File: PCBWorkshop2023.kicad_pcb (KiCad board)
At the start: 2 copper layers, 70 x 38 mm, 10 parts, among them J1 Neopixel, J2 I2C, SW1 POWER SELECT, U1 TP4056, U2 WeMos_D1_mini

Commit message: Initial Routing
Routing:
- net +3V3: track 0.00 -> 59.1 mm, vias 0 -> 2
- net +4V: track 0.00 -> 47.6 mm
- net Neopixel: track 0.00 -> 34.6 mm
- net Net-(SW1-Pad1): track 0.00 -> 26.3 mm
- net Net-(BT1-Pad2): track 0.00 -> 22.8 mm
- net Net-(BT1-Pad1): track 0.00 -> 20.0 mm
- net I2C_SDA: track 0.00 -> 17.4 mm
- net I2C_CLK: track 0.00 -> 13.9 mm
- net +5V: track 0.00 -> 7.76 mm
- net (no net): track 0.00 -> 0.64 mm
- added copper zone on B.Cu, net GND
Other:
- board text added: "TODO: - Rounded corners - 90° angled switch footprint (Pusterla) - Cutout for Antenna area"
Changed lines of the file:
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@@
   )
   (gr_rect (start 111 99) (end 181 61) (layer "Edge.Cuts") (width 0.1) (fill none))
+  (gr_text "TODO:\n\n- Rounded corners\n- 90° angled switch footprint (Pusterla)\n- Cutout for Antenna area" (at 69 63) (layer "F.SilkS")
+    (effects (font (size 1 1) (thickness 0.15)) (justify left))
+  )
+  (segment (start 176.75 75.1075) (end 176.1075 75.1075) (width 0.6) (layer "B.Cu") (net 0))
+  (segment (start 165.54 62) (end 164 62) (width 1) (layer "B.Cu") (net 2))
+  (segment (start 164 62) (end 162 64) (width 1) (layer "B.Cu") (net 2))
+  (segment (start 162 64) (end 162 68) (width 1) (layer "B.Cu") (net 2))
+  (segment (start 147.3 82.7) (end 144.68 82.7) (width 1) (layer "B.Cu") (net 2))
+  (segment (start 167.54 64) (end 165.54 62) (width 1) (layer "B.Cu") (net 2))
+  (segment (start 162 68) (end 147.3 82.7) (width 1) (layer "B.Cu") (net 2))
+  (segment (start 165 66.6575) (end 165 64) (width 1) (layer "B.Cu") (net 3))
+  (segment (start 165 67.46) (end 144.68 87.78) (width 1) (layer "B.Cu") (net 3))
+  (segment (start 165 66.6575) (end 165 67.46) (width 1) (layer "B.Cu") (net 3))
+  (segment (start 174.85 73.7075) (end 174.85 72.027601) (width 1) (layer "B.Cu") (net 3))
+  (segment (start 174.85 72.027601) (end 170.282399 67.46) (width 1) (layer "B.Cu") (net 3))
+  (segment (start 173.45 75.1075) (end 174.85 73.7075) (width 1) (layer "B.Cu") (net 3))
+  (segment (start 170.282399 67.46) (end 165 67.46) (width 1) (layer "B.Cu") (net 3))
+  (segment (start 157 69) (end 157 68) (width 1) (layer "F.Cu") (net 4))
+  (segment (start 157 79) (end 157 69) (width 1) (layer "F.Cu") (net 4))
+  (via (at 157 79) (size 3) (drill 1.1) (layers "F.Cu" "B.Cu") (net 4))
+  (via (at 157 68) (size 3) (drill 1.1) (layers "F.Cu" "B.Cu") (net 4))
+  (segment (start 157 68) (end 157 64.54) (width 1) (layer "B.Cu") (net 4))
+  (segment (start 149 91) (end 156.46 83.54) (width 1) (layer "B.Cu") (net 4))
+  (segment (start 125.04 91) (end 149 91) (width 1) (layer "B.Cu") (net 4))
+  (segment (start 156.46 83.54) (end 157 83) (width 1) (layer "B.Cu") (net 4))
+  (segment (start 157 83) (end 157 79) (width 1) (layer "B.Cu") (net 4))
+  (segment (start 157 64.54) (end 156.46 64) (width 1) (layer "B.Cu") (net 4))
+  (segment (start 121.82 87.78) (end 125.04 91) (width 1) (layer "B.Cu") (net 4))
+  (segment (start 149 73.3) (end 149 68.92) (width 0.6) (layer "B.Cu") (net 5))
+  (segment (start 149 68.92) (end 153.92 64) (width 0.6) (layer "B.Cu") (net 5))
+  (segment (start 144.68 77.62) (end 149 73.3) (width 0.6) (layer "B.Cu") (net 5))
+  (segment (start 144.68 75.08) (end 148.200499 71.559501) (width 0.6) (layer "B.Cu") (net 6))
+  (segment (start 148.200499 71.559501) (end 148.200499 67.179501) (width 0.6) (layer "B.Cu") (net 6))
+  (segment (start 148.200499 67.179501) (end 151.38 64) (width 0.6) (layer "B.Cu") (net 6))
+  (segment (start 170.6075 72.6075) (end 169.5875 71.5875) (width 1) (layer "B.Cu") (net 7))
+  (segment (start 169.5875 71.5875) (end 166.1125 71.5875) (width 1) (layer "B.Cu") (net 7))
+  (segment (start 173.45 72.6075) (end 170.6075 72.6075) (width 1) (layer "B.Cu") (net 7))
+  (segment (start 170.5125 94.4875) (end 178 87) (width 1) (layer "B.Cu") (net 8))
+  (segment (start 178 82.1575) (end 173.45 77.6075) (width 1) (layer "B.Cu") (net 8))
+  (segment (start 166.1125 94.4875) (end 170.5125 94.4875) (width 1) (layer "B.Cu") (net 8))
+  (segment (start 178 87) (end 178 82.1575) (width 1) (layer "B.Cu") (net 8))
+  (segment (start 176.1 84.3) (end 172.4 88) (width 1) (layer "B.Cu") (net 9))
+  (segment (start 172.4 88) (end 165.130666 88) (width 1) (layer "B.Cu") (net 9))
+  (segment (start 165.130666 88) (end 162.6125 90.518166) (width 1) (layer "B.Cu") (net 9))
+  (segment (start 162.6125 90.518166) (end 162.6125 94.4875) (width 1) (layer "B.Cu") (net 9))
+  (segment (start 155.0125 94.4875) (end 156.5125 94.4875) (width 1) (layer "B.Cu") (net 10))
+  (segment (start 166.7 84.3) (end 173.6 84.3) (width 1) (layer "B.Cu") (net 10))
+  (segment (start 156.5125 94.4875) (end 166.7 84.3) (width 1) (layer "B.Cu") (net 10))
+  (zone (net 1) (net_name "GND") (layer "B.Cu") (hatch edge 0.508)
+    (connect_pads (clearance 0.508))
+    (min_thickness 0.254) (filled_areas_thickness no)
+    (fill yes (thermal_gap 0.508) (thermal_bridge_width 0.508))
+    (polygon
+      (pts
+        (xy 184 104)
+        (xy 105 104)
+        (xy 105 57)
+        (xy 184 57)
+      )
+    )
+  )
 )

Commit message: Changes with Bernd
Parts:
- added J3: Conn_01x02, Connector_PinHeader_2.54mm:PinHeader_1x02_P2.54mm_Vertical, F.Cu at (172.0, 63.0)
- added J4: Conn_01x07, Connector_PinHeader_2.54mm:PinHeader_1x07_P2.54mm_Vertical, F.Cu at (120.2, 89.3)
- J2: footprint Connector_PinHeader_2.54mm:PinHeader_1x04_P2.54mm_Vertical -> Connector_PinHeader_2.00mm:PinHeader_1x04_P2.00mm_Vertical
- moved SW1 16.5 mm to (189.7, 74.5)
- moved J1 5.18 mm to (165.0, 63.0)
- moved J2 3.16 mm to (156.0, 63.0)
- moved U2 1.55 mm to (123.0, 69.0)
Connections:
- U2 pad 1: unconnected-(U2-Pad1) -> DEEPSLEEP
- U2 pad 2: unconnected-(U2-Pad2) -> Net-(U2-Pad2)
- U2 pad 3: unconnected-(U2-Pad3) -> DEEPSLEEP
- U2 pad 4: unconnected-(U2-Pad4) -> Net-(U2-Pad4)
- U2 pad 5: unconnected-(U2-Pad5) -> Net-(U2-Pad5)
- U2 pad 6: unconnected-(U2-Pad6) -> Net-(U2-Pad6)
- U2 pad 7: unconnected-(U2-Pad7) -> Net-(U2-Pad7)
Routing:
- net DEEPSLEEP: track 0.00 -> 10.2 mm
- net +5V: track 7.76 -> 16.4 mm
- net +3V3: track 59.1 -> 64.4 mm
- net Net-(U2-Pad2): track 0.00 -> 4.64 mm
- net Net-(U2-Pad7): track 0.00 -> 2.86 mm
- net Net-(U2-Pad5): track 0.00 -> 2.86 mm
- net Net-(U2-Pad6): track 0.00 -> 2.86 mm
- net Net-(U2-Pad4): track 0.00 -> 2.86 mm
- net +4V: track 47.6 -> 49.1 mm
- net I2C_SDA: track 17.4 -> 16.2 mm
- net I2C_CLK: track 13.9 -> 12.8 mm
- net (no net): track 0.64 -> 0.00 mm
- net Neopixel: track 34.6 -> 34.1 mm
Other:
- board size 70 x 38 mm -> 70 x 39 mm
- board text added: "TODO: - Rounded corners - 90° angled switch footprint (Pusterla) - Double check Groove I2C adapter"
- board text removed: "TODO: - Rounded corners - 90° angled switch footprint (Pusterla) - Cutout for Antenna area"

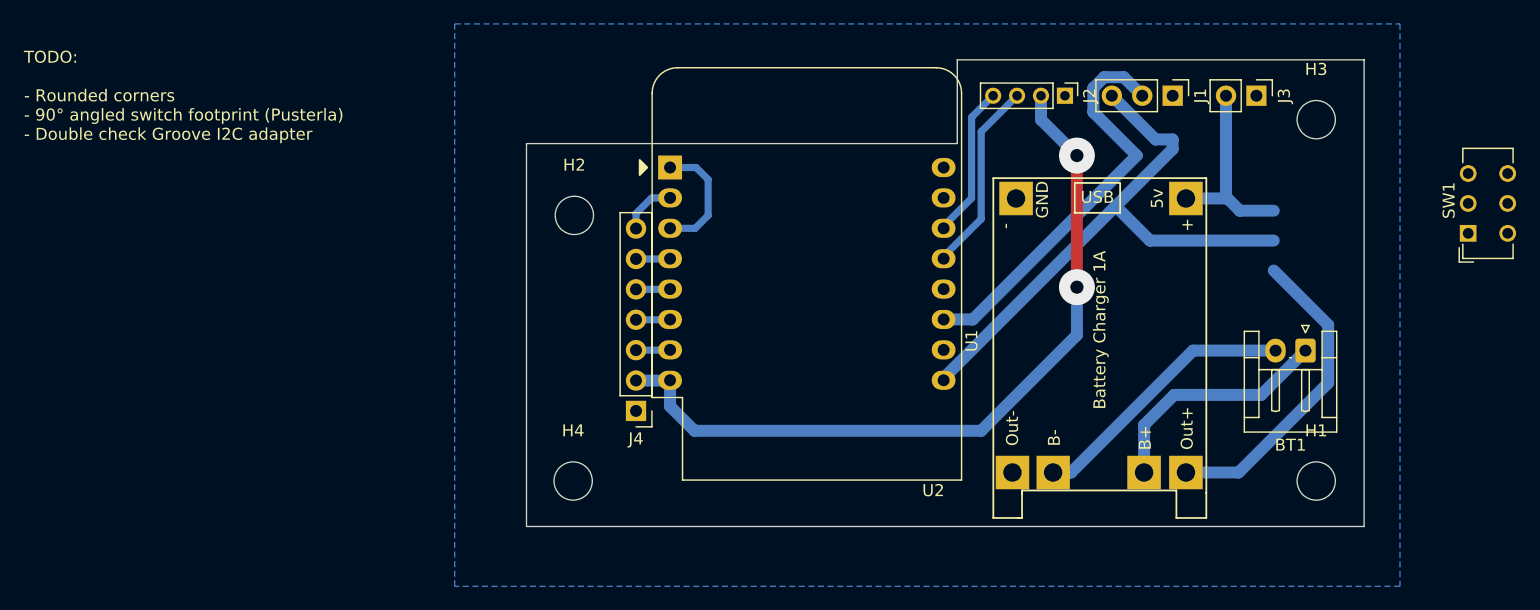
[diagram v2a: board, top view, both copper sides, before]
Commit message: Rounded corners and switch
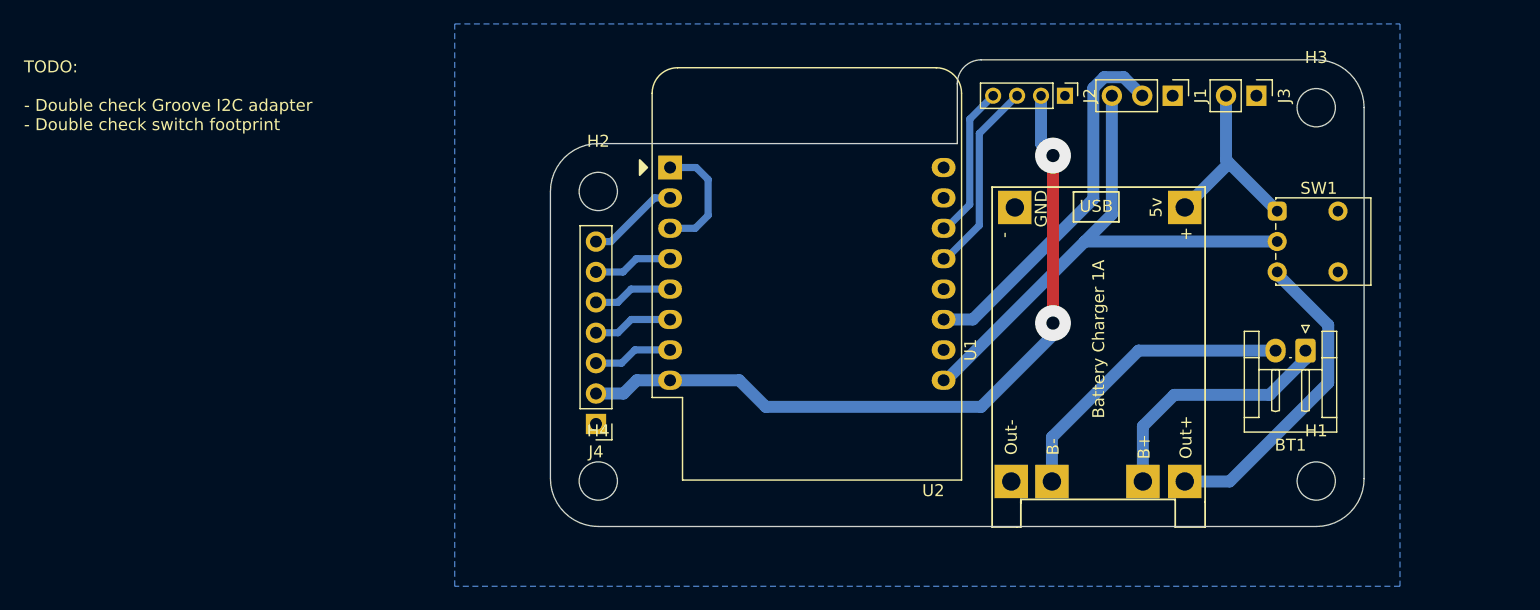
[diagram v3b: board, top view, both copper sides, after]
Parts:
- J4: value Conn_01x07 -> Connections
- SW1: footprint Button_Switch_THT:SW_CuK_JS202011CQN_DPDT_Straight -> Button_Switch_THT:SW_Push_1P2T_Vertical_E-Switch_800UDP8P1A1M6
- moved SW1 16.1 mm to (173.7, 72.6), turned to 0 degrees
- moved J4 3.52 mm to (116.8, 90.4)
- moved H2 2.83 mm to (117.0, 71.0)
- moved H4 2.10 mm to (117.0, 95.2)
- moved H3 1.00 mm to (177.0, 64.0)
- moved U1 0.76 mm to (167.7, 70.6)
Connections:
- SW1 pad 1: Net-(SW1-Pad1) -> +5V
- SW1 pad 3: +5V -> Net-(U1-Pad3)
- U1 pad 3: Net-(SW1-Pad1) -> Net-(U1-Pad3)
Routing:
- net Net-(U1-Pad3): track 0.00 -> 26.7 mm
- net Net-(SW1-Pad1): track 26.3 -> 0.00 mm
- net Net-(J4-Pad4): track 2.86 -> 6.65 mm
- net Net-(J4-Pad5): track 2.86 -> 6.65 mm
- net Net-(J4-Pad3): track 2.86 -> 6.65 mm
- net Net-(J4-Pad6): track 2.86 -> 6.65 mm
- net +4V: track 49.1 -> 46.0 mm
- net Net-(J4-Pad7): track 4.64 -> 7.70 mm
- net Neopixel: track 34.1 -> 31.1 mm
- net Net-(BT1-Pad2): track 22.8 -> 25.4 mm
- net +3V3: track 64.4 -> 62.5 mm
- net Net-(BT1-Pad1): track 20.0 -> 21.2 mm
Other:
- board size 70 x 39 mm -> 68 x 39 mm
- board text added: "TODO: - Double check Groove I2C adapter - Double check switch footprint"
- board text removed: "TODO: - Rounded corners - 90° angled switch footprint (Pusterla) - Double check Groove I2C adapter"

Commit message: Prepare for milling
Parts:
- added D1: 1N4001, Diode_THT:D_A-405_P7.62mm_Horizontal, F.Cu at (169.8, 68.7)
- SW1: value POWER SELECT -> POWER
- moved BT1 3.30 mm to (176.1, 81.0)
- moved U1 2.64 mm to (167.7, 68.0)
- moved J2 1.14 mm to (155.0, 63.5)
- moved U2 1.05 mm to (122.0, 68.9)
- moved SW1 0.98 mm to (173.0, 72.0)
- moved J1 0.80 mm to (165.1, 63.8)
- moved J3 0.75 mm to (172.0, 63.8)
- moved J4 0.37 mm to (117.0, 90.8)
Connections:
- J1 pad 3: +4V -> +5V
- J3 pad 2: +5V -> Net-(J3-Pad2)
- SW1 pad 3: Net-(U1-Pad3) -> (no net)
- U1 pad 1: +5V -> Net-(J3-Pad2)
- U1 pad 3: Net-(U1-Pad3) -> +4V
- U2 pad 9: +4V -> +5V
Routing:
- net +5V: track 16.7 -> 52.7 mm
- net Net-(U1-Pad3): track 26.7 -> 0.00 mm
- net +4V: track 46.0 -> 30.6 mm
- net Net-(J3-Pad2): track 0.00 -> 9.19 mm
- net Neopixel: track 31.1 -> 34.0 mm
- net Net-(BT1-Pad2): track 25.4 -> 23.5 mm
- net Net-(J4-Pad5): track 6.65 -> 5.58 mm
- net Net-(J4-Pad3): track 6.65 -> 5.58 mm
- net Net-(J4-Pad4): track 6.65 -> 5.58 mm
- net Net-(J4-Pad6): track 6.65 -> 5.58 mm
- net Net-(J4-Pad7): track 7.70 -> 6.64 mm

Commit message: Improvements
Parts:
- added C1: C_Polarized, Capacitor_THT:C_Radial_D6.3mm_H11.0mm_P2.50mm, F.Cu at (162.8, 68.3)
- moved U1 3.75 mm to (167.7, 71.8)
- moved J3 1.12 mm to (172.0, 62.6)
- moved J2 1.09 mm to (155.0, 62.5)
- moved J1 0.80 mm to (165.0, 63.0)
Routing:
- net +5V: track 52.7 -> 60.4 mm
- net Net-(BT1-Pad1): track 21.3 -> 25.1 mm
- net Net-(BT1-Pad2): track 23.5 -> 27.3 mm
- net Net-(D1-Pad1): track 9.19 -> 12.6 mm
- net +4V: track 30.6 -> 32.9 mm
- net GND: track 0.00 -> 0.63 mm
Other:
- board text added: "TODO: - Check Groove I2C adapter orientation"
- board text removed: "TODO: - Double check Groove I2C adapter - Double check switch footprint"
